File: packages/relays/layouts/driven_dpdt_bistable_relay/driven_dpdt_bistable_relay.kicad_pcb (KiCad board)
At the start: 2 copper layers, 9 parts

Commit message: Update build script and regenerate outputs
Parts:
- R1, R3: value 10kΩ ±1% 62.5mW -> 1kΩ ±1% 62.5mW
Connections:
- C5 pad 1: hv -> hv-1
- C5 pad 2: gnd-1 -> gnd
- C6 pad 1: hv -> hv-1
- C6 pad 2: gnd-1 -> gnd
- C8 pad 1: hv-1 -> hv
- C8 pad 2: gnd -> gnd-1
- D1 pad 2: line-5 -> line-7
- D2 pad 2: line-1 -> line-6
- R1 pad 2: gnd-1 -> gnd
- R3 pad 2: gnd-1 -> gnd
- RELAY1 pad 1: gnd -> gnd-1
- RELAY1 pad 2: line-6 -> line-4
- RELAY1 pad 3: line -> line-5
- RELAY1 pad 4: line-4 -> line-3
- RELAY1 pad 5: line-2 -> line
- RELAY1 pad 6: line-7 -> line-1
- RELAY1 pad 7: line-3 -> line-2
- RELAY1 pad 8: hv-1 -> hv
- U7 pad 2: line-5 -> line-7
- U7 pad 3: line-1 -> line-6
- U7 pad 4: hv -> hv-1
- U7 pad 5: gnd -> gnd-1
- U7 pad 6: gnd-1 -> gnd
- U7 pad 7: gnd-1 -> gnd
- U7 pad 8: hv-1 -> hv
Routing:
- net gnd-1: track 0.00 -> 6.34 mm
- net gnd: track 6.34 -> 0.00 mm
- net line-7: track 0.00 -> 4.81 mm
- net line-6: track 0.00 -> 4.81 mm
- net line-5: track 4.81 -> 0.00 mm
- net line-1: track 4.81 -> 0.00 mm
- net hv-1: track 6.34 -> 2.61 mm
- net hv: track 2.61 -> 6.34 mm
- added copper zone on F.Cu, net gnd
- removed copper zone on F.Cu, net gnd-1
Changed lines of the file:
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@@
     )
     (net 0 "")
-    (net 1 "line-3")
+    (net 1 "line-2")
     (net 2 "net")
-    (net 3 "gnd")
-    (net 4 "line-7")
-    (net 5 "line")
-    (net 6 "line-2")
-    (net 7 "hv-1")
-    (net 8 "line-6")
-    (net 9 "line-4")
+    (net 3 "gnd-1")
+    (net 4 "line-1")
+    (net 5 "line-5")
+    (net 6 "line")
+    (net 7 "hv")
+    (net 8 "line-4")
+    (net 9 "line-3")
     (net 10 "led_indicator_b.led-cathode")
     (net 11 "led_indicator_a.led-cathode")
-    (net 12 "line-1")
-    (net 13 "line-5")
-    (net 14 "hv")
-    (net 15 "gnd-1")
+    (net 12 "line-6")
+    (net 13 "line-7")
+    (net 14 "hv-1")
+    (net 15 "gnd")
     (footprint "atopile:LED0603-RD-c81ffb"
         (layer "F.Cu")
@@
             (size 0.8 0.8)
             (layers "F.Cu" "F.Mask" "F.Paste")
-            (net 13 "line-5")
+            (net 13 "line-7")
         )
         (embedded_fonts no)
@@
             )
         )
-        (property "Value" "10kΩ ±1% 62.5mW"
+        (property "Value" "1kΩ ±1% 62.5mW"
             (at 0 4 90)
             (layer "F.Fab")
@@
             )
         )
-        (property "LCSC" "C25744"
-            (at 0 0 90)
-            (layer "User.9")
-            (hide yes)
-            (effects
-                (font
-                    (size 0.125 0.125)
-                    (thickness 0.01875)
-                )
-            )
-        )
-        (property "Partnumber" "0402WGF1002TCE"
+        (property "LCSC" "C11702"
+            (at 0 0 90)
+            (layer "User.9")
+            (hide yes)
+            (effects
+                (font
+                    (size 0.125 0.125)
+                    (thickness 0.01875)
+                )
+            )
+        )
+        (property "Partnumber" "0402WGF1001TCE"
             (at 0 0 90)
             (layer "User.9")
@@
             )
         )
-        (property "JLCPCB description" "62.5mW Thick Film Resistors 50V ±100ppm/℃ ±1% 10kΩ 0402 Chip Resistor - Surface Mount ROHS"
+        (property "JLCPCB description" "62.5mW Thick Film Resistors 50V ±100ppm/℃ ±1% 1kΩ 0402 Chip Resistor - Surface Mount ROHS"
             (at 0 0 90)
             (layer "User.9")
@@
             )
         )
-        (property "PARAM_resistance" "{\"type\": \"Quantity_Interval_Disjoint\", \"data\": {\"intervals\": {\"type\": \"Numeric_Interval_Disjoint\", \"data\": {\"intervals\": [{\"type\": \"Numeric_Interval\", \"data\": {\"min\": 9900.000002235174, \"max\": 10099.999997764826}}]}}, \"unit\": \"ohm\"}}"
+        (property "PARAM_resistance" "{\"type\": \"Quantity_Interval_Disjoint\", \"data\": {\"intervals\": {\"type\": \"Numeric_Interval_Disjoint\", \"data\": {\"intervals\": [{\"type\": \"Numeric_Interval\", \"data\": {\"min\": 990.0000002235174, \"max\": 1009.9999997764826}}]}}, \"unit\": \"ohm\"}}"
             (at 0 0 0)
             (layer "User.9")
@@
             (size 0.57 0.54)
             (layers "F.Cu" "F.Mask" "F.Paste")
-            (net 15 "gnd-1")
+            (net 15 "gnd")
         )
         (embedded_fonts no)
@@
             (size 0.79 0.54)
             (layers "F.Cu" "F.Mask" "F.Paste")
-            (net 7 "hv-1")
+            (net 7 "hv")
         )
         (pad "2" smd rect
@@
             (size 0.79 0.54)
             (layers "F.Cu" "F.Mask" "F.Paste")
-            (net 3 "gnd")
+            (net 3 "gnd-1")
         )
         (embedded_fonts no)
@@
             (size 0.79 0.54)
             (layers "F.Cu" "F.Mask" "F.Paste")
-            (net 14 "hv")
+            (net 14 "hv-1")
         )
         (pad "2" smd rect
@@
             (size 0.79 0.54)
             (layers "F.Cu" "F.Mask" "F.Paste")
-            (net 15 "gnd-1")
+            (net 15 "gnd")
         )
         (embedded_fonts no)
@@
             (size 0.63 1.86)
             (layers "F.Cu" "F.Mask" "F.Paste")
-            (net 13 "line-5")
+            (net 13 "line-7")
         )
         (pad "3" smd oval
@@
             (size 0.63 1.86)
             (layers "F.Cu" "F.Mask" "F.Paste")
-            (net 12 "line-1")
+            (net 12 "line-6")
         )
         (pad "4" smd oval
@@
             (size 0.63 1.86)
             (layers "F.Cu" "F.Mask" "F.Paste")
-            (net 14 "hv")
+            (net 14 "hv-1")
         )
         (pad "5" smd oval
@@
             (size 0.63 1.86)
             (layers "F.Cu" "F.Mask" "F.Paste")
-            (net 3 "gnd")
+            (net 3 "gnd-1")
         )
         (pad "6" smd oval
@@
             (size 0.63 1.86)
             (layers "F.Cu" "F.Mask" "F.Paste")
-            (net 15 "gnd-1")
+            (net 15 "gnd")
         )
         (pad "7" smd oval
@@
             (size 0.63 1.86)
             (layers "F.Cu" "F.Mask" "F.Paste")
-            (net 15 "gnd-1")
+            (net 15 "gnd")
         )
         (pad "8" smd oval
@@
             (size 0.63 1.86)
             (layers "F.Cu" "F.Mask" "F.Paste")
-            (net 7 "hv-1")
+            (net 7 "hv")
         )
         (embedded_fonts no)
@@
             )
         )
-        (property "Value" "10kΩ ±1% 62.5mW"
+        (property "Value" "1kΩ ±1% 62.5mW"
             (at 0 4 90)
             (layer "F.Fab")
@@
             )
         )
-        (property "LCSC" "C25744"
-            (at 0 0 90)
-            (layer "User.9")
-            (hide yes)
-            (effects
-                (font
-                    (size 0.125 0.125)
-                    (thickness 0.01875)
-                )
-            )
-        )
-        (property "Partnumber" "0402WGF1002TCE"
+        (property "LCSC" "C11702"
+            (at 0 0 90)
+            (layer "User.9")
+            (hide yes)
+            (effects
+                (font
+                    (size 0.125 0.125)
+                    (thickness 0.01875)
+                )
+            )
+        )
+        (property "Partnumber" "0402WGF1001TCE"
             (at 0 0 90)
             (layer "User.9")
@@
             )
         )
-        (property "JLCPCB description" "62.5mW Thick Film Resistors 50V ±100ppm/℃ ±1% 10kΩ 0402 Chip Resistor - Surface Mount ROHS"
+        (property "JLCPCB description" "62.5mW Thick Film Resistors 50V ±100ppm/℃ ±1% 1kΩ 0402 Chip Resistor - Surface Mount ROHS"
             (at 0 0 90)
             (layer "User.9")
@@
             )
         )
-        (property "PARAM_resistance" "{\"type\": \"Quantity_Interval_Disjoint\", \"data\": {\"intervals\": {\"type\": \"Numeric_Interval_Disjoint\", \"data\": {\"intervals\": [{\"type\": \"Numeric_Interval\", \"data\": {\"min\": 9900.000002235174, \"max\": 10099.999997764826}}]}}, \"unit\": \"ohm\"}}"
+        (property "PARAM_resistance" "{\"type\": \"Quantity_Interval_Disjoint\", \"data\": {\"intervals\": {\"type\": \"Numeric_Interval_Disjoint\", \"data\": {\"intervals\": [{\"type\": \"Numeric_Interval\", \"data\": {\"min\": 990.0000002235174, \"max\": 1009.9999997764826}}]}}, \"unit\": \"ohm\"}}"
             (at 0 0 0)
             (layer "User.9")
@@
             (size 0.57 0.54)
             (layers "F.Cu" "F.Mask" "F.Paste")
-            (net 15 "gnd-1")
+            (net 15 "gnd")
         )
         (embedded_fonts no)
@@
             (size 0.8 0.8)
             (layers "F.Cu" "F.Mask" "F.Paste")
-            (net 12 "line-1")
+            (net 12 "line-6")
         )
         (embedded_fonts no)
@@
             (size 0.79 0.54)
             (layers "F.Cu" "F.Mask" "F.Paste")
-            (net 14 "hv")
+            (net 14 "hv-1")
         )
         (pad "2" smd rect
@@
             (size 0.79 0.54)
             (layers "F.Cu" "F.Mask" "F.Paste")
-            (net 15 "gnd-1")
+            (net 15 "gnd")
         )
         (embedded_fonts no)
@@
             (size 0.8 1.8)
             (layers "F.Cu" "F.Mask" "F.Paste")
-            (net 3 "gnd")
+            (net 3 "gnd-1")
         )
         (pad "2" smd rect
@@
             (size 0.8 1.8)
             (layers "F.Cu" "F.Mask" "F.Paste")
-            (net 8 "line-6")
+            (net 8 "line-4")
         )
         (pad "3" smd rect
@@
             (size 0.8 1.8)
             (layers "F.Cu" "F.Mask" "F.Paste")
-            (net 5 "line")
+            (net 5 "line-5")
         )
         (pad "4" smd rect
@@
             (size 0.8 1.8)
             (layers "F.Cu" "F.Mask" "F.Paste")
-            (net 9 "line-4")
+            (net 9 "line-3")
         )
         (pad "5" smd rect
@@
             (size 0.8 1.8)
             (layers "F.Cu" "F.Mask" "F.Paste")
-            (net 6 "line-2")
+            (net 6 "line")
         )
         (pad "6" smd rect
@@
             (size 0.8 1.8)
             (layers "F.Cu" "F.Mask" "F.Paste")
-            (net 4 "line-7")
+            (net 4 "line-1")
         )
         (pad "7" smd rect
@@
             (size 0.8 1.8)
             (layers "F.Cu" "F.Mask" "F.Paste")
-            (net 1 "line-3")
+            (net 1 "line-2")
         )
         (pad "8" smd rect
@@
             (size 0.8 1.8)
             (layers "F.Cu" "F.Mask" "F.Paste")
-            (net 7 "hv-1")
+            (net 7 "hv")
         )
         (embedded_fonts no)
@@
     (zone
         (net 15)
-        (net_name "gnd-1")
+        (net_name "gnd")
         (layers "F.Cu")
         (hatch edge 0.5)

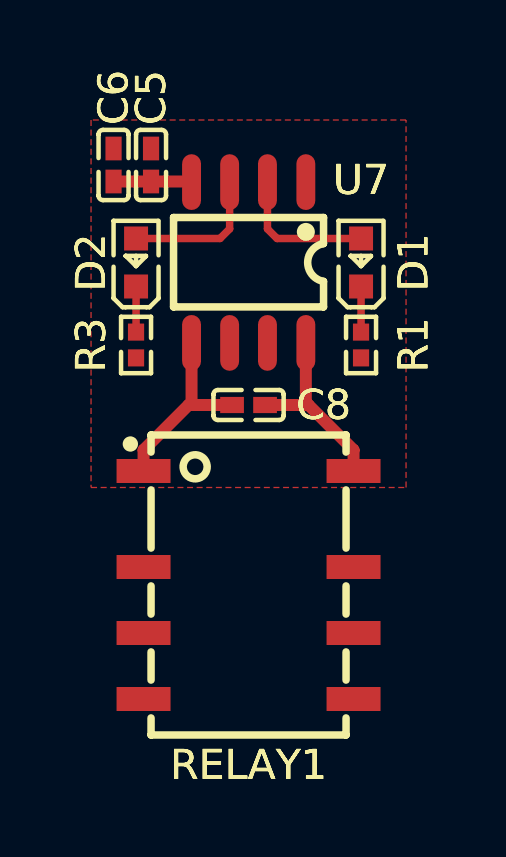
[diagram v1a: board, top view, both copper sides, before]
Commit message: Build all packages without designators on silkscreen.
Also disable fail_on_drc and enable keep_picked_parts for build
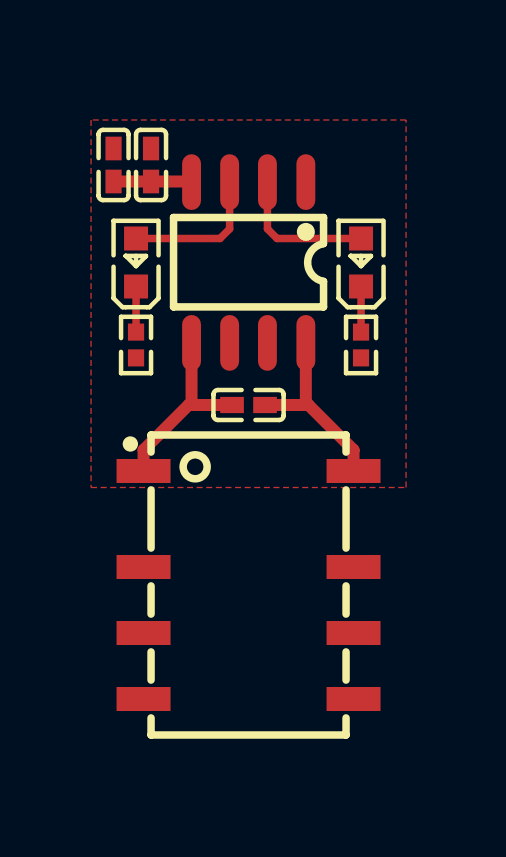
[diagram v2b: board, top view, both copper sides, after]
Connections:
- D1 pad 2: line-7 -> line
- D2 pad 2: line-6 -> line-4
- RELAY1 pad 2: line-4 -> line-3
- RELAY1 pad 3: line-5 -> line-1
- RELAY1 pad 4: line-3 -> line-7
- RELAY1 pad 5: line -> line-2
- RELAY1 pad 6: line-1 -> line-6
- RELAY1 pad 7: line-2 -> line-5
- U7 pad 2: line-7 -> line
- U7 pad 3: line-6 -> line-4
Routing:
- net line-7: track 4.81 -> 0.00 mm
- net line-6: track 4.81 -> 0.00 mm
- net line-4: track 0.00 -> 4.81 mm
- net line: track 0.00 -> 4.81 mm
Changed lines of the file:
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@@
     )
     (net 0 "")
-    (net 1 "line-2")
+    (net 1 "line-5")
     (net 2 "net")
     (net 3 "gnd-1")
-    (net 4 "line-1")
-    (net 5 "line-5")
-    (net 6 "line")
+    (net 4 "line-6")
+    (net 5 "line-1")
+    (net 6 "line-2")
     (net 7 "hv")
-    (net 8 "line-4")
-    (net 9 "line-3")
+    (net 8 "line-3")
+    (net 9 "line-7")
     (net 10 "led_indicator_b.led-cathode")
     (net 11 "led_indicator_a.led-cathode")
-    (net 12 "line-6")
-    (net 13 "line-7")
+    (net 12 "line-4")
+    (net 13 "line")
     (net 14 "hv-1")
     (net 15 "gnd")
@@
             (at 0 1.75 90)
             (layer "F.SilkS")
-            (hide no)
+            (hide yes)
             (effects
                 (font
@@
                     (thickness 0.15)
                 )
+                (hide yes)
             )
             (unlocked no)
@@
                     (thickness 0.15)
                 )
+                (hide yes)
             )
             (unlocked no)
@@
             (size 0.8 0.8)
             (layers "F.Cu" "F.Mask" "F.Paste")
-            (net 13 "line-7")
+            (net 13 "line")
         )
         (embedded_fonts no)
@@
             (at 0 -1.75 90)
             (layer "F.SilkS")
-            (hide no)
+            (hide yes)
             (effects
                 (font
@@
                     (thickness 0.15)
                 )
+                (hide yes)
             )
             (unlocked no)
@@
                     (thickness 0.15)
                 )
+                (hide yes)
             )
             (unlocked no)
@@
             (at -2.5 0 0)
             (layer "F.SilkS")
-            (hide no)
+            (hide yes)
             (effects
                 (font
@@
                     (thickness 0.15)
                 )
+                (hide yes)
             )
             (unlocked no)
@@
                     (thickness 0.15)
                 )
+                (hide yes)
             )
             (unlocked no)
@@
             (at 2.25 0 90)
             (layer "F.SilkS")
-            (hide no)
+            (hide yes)
             (effects
                 (font
@@
                     (thickness 0.15)
                 )
+                (hide yes)
             )
             (unlocked no)
@@
                     (thickness 0.15)
                 )
+                (hide yes)
             )
             (unlocked no)
@@
             (at -3.75 2.75 0)
             (layer "F.SilkS")
-            (hide no)
+            (hide yes)
             (effects
                 (font
@@
                     (thickness 0.15)
                 )
+                (hide yes)
             )
             (unlocked no)
@@
                     (thickness 0.15)
                 )
+                (hide yes)
             )
             (unlocked no)
@@
             (size 0.63 1.86)
             (layers "F.Cu" "F.Mask" "F.Paste")
-            (net 13 "line-7")
+            (net 13 "line")
         )
         (pad "3" smd oval
@@
             (size 0.63 1.86)
             (layers "F.Cu" "F.Mask" "F.Paste")
-            (net 12 "line-6")
+            (net 12 "line-4")
         )
         (pad "4" smd oval
@@
             (at 0 1.5 90)
             (layer "F.SilkS")
-            (hide no)
+            (hide yes)
             (effects
                 (font
@@
                     (thickness 0.15)
                 )
+                (hide yes)
             )
             (unlocked no)
@@
                     (thickness 0.15)
                 )
+                (hide yes)
             )
             (unlocked no)
@@
             (at 0 -1.5 90)
             (layer "F.SilkS")
-            (hide no)
+            (hide yes)
             (effects
                 (font
@@
                     (thickness 0.15)
                 )
+                (hide yes)
             )
             (unlocked no)
@@
                     (thickness 0.15)
                 )
+                (hide yes)
             )
             (unlocked no)
@@
             (size 0.8 0.8)
             (layers "F.Cu" "F.Mask" "F.Paste")
-            (net 12 "line-6")
+            (net 12 "line-4")
         )
         (embedded_fonts no)
@@
             (at 2.25 0 90)
             (layer "F.SilkS")
-            (hide no)
+            (hide yes)
             (effects
                 (font
@@
                     (thickness 0.15)
                 )
+                (hide yes)
             )
             (unlocked no)
@@
                     (thickness 0.15)
                 )
+                (hide yes)
             )
             (unlocked no)
@@
             (at 6 0 0)
             (layer "F.SilkS")
-            (hide no)
+            (hide yes)
             (effects
                 (font
@@
                     (thickness 0.15)
                 )
+                (hide yes)
             )
             (unlocked no)
@@
                     (thickness 0.15)
                 )
+                (hide yes)
             )
             (unlocked no)
@@
             (size 0.8 1.8)
             (layers "F.Cu" "F.Mask" "F.Paste")
-            (net 8 "line-4")
+            (net 8 "line-3")
         )
         (pad "3" smd rect
@@
             (size 0.8 1.8)
             (layers "F.Cu" "F.Mask" "F.Paste")
-            (net 5 "line-5")
+            (net 5 "line-1")
         )
         (pad "4" smd rect
@@
             (size 0.8 1.8)
             (layers "F.Cu" "F.Mask" "F.Paste")
-            (net 9 "line-3")
+            (net 9 "line-7")
         )
         (pad "5" smd rect
@@
             (size 0.8 1.8)
             (layers "F.Cu" "F.Mask" "F.Paste")
-            (net 6 "line")
+            (net 6 "line-2")
         )
         (pad "6" smd rect
@@
             (size 0.8 1.8)
             (layers "F.Cu" "F.Mask" "F.Paste")
-            (net 4 "line-1")
+            (net 4 "line-6")
         )
         (pad "7" smd rect
@@
             (size 0.8 1.8)
             (layers "F.Cu" "F.Mask" "F.Paste")
-            (net 1 "line-2")
+            (net 1 "line-5")
         )
         (pad "8" smd rect
